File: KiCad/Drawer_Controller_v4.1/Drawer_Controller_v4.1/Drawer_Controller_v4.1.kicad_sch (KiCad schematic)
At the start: 21 parts, among them J1 Conn_02x05_Odd_Even, J2 Conn_02x03_Odd_Even, J3 Conn_02x04_Odd_Even, U1 PESD2CANFD24L-TR, X1 RJ45_45_degree_angled, X2 Conn_01x02_2.5mm_JST_S02B-XAS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, X3 Conn_01x08_2.5mm_JST_S04B-XAS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, X4 Conn_02x03_3.0mm_Molex_Micro_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, X5 Conn_01x03_2.5mm_JST_S04B-XAS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, X6 Conn_01x04_2.5mm_JST_S04B-XAS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

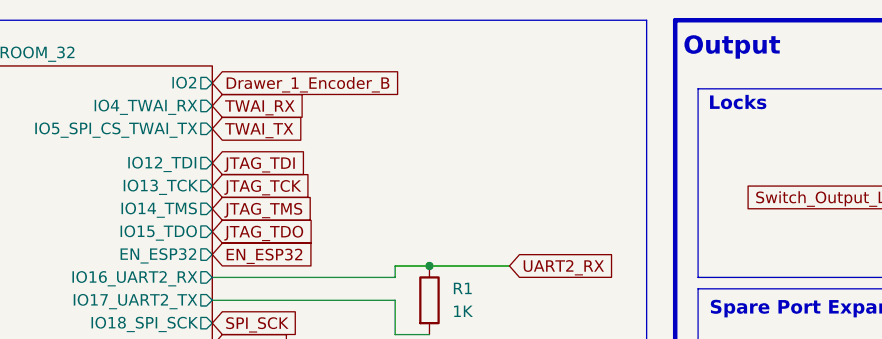
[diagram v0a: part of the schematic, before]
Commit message: fix: adds important hint about usage of IO2 for flashing the ESP32
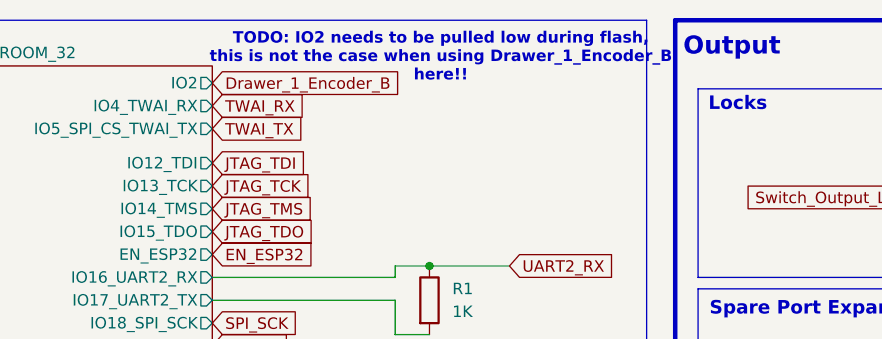
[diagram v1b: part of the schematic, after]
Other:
- note added: "TODO: IO2 needs to be pulled low during flash, this is not the case when using Drawer_1_Encoder_B here!!"
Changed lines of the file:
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@@
+		)
+	)
+	(text "TODO: IO2 needs to be pulled low during flash,\nthis is not the case when using Drawer_1_Encoder_B\nhere!!"
+		(exclude_from_sim no)
+		(at 219.71 18.796 0)
+		(effects
+			(font
+				(size 1.27 1.27)
+				(thickness 0.254)
+				(bold yes)
+				(color 255 0 0 1)
+			)
 		)
 	)

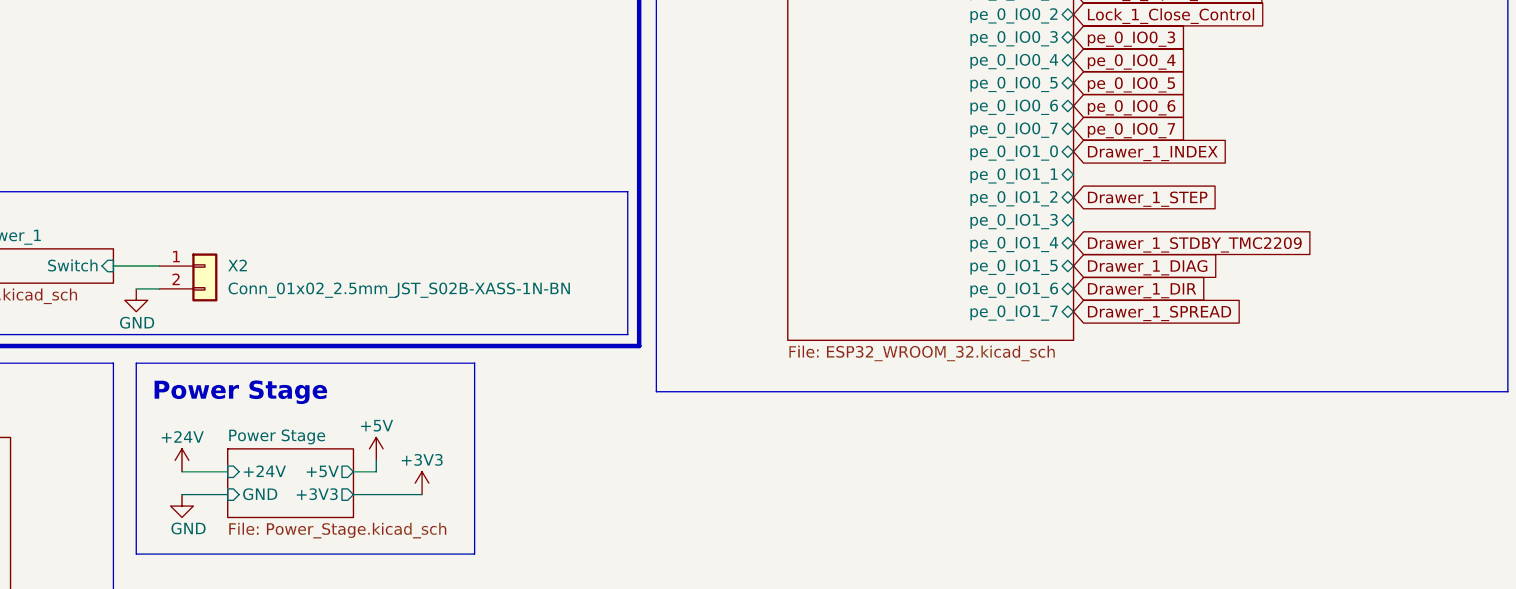
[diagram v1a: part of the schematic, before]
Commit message: fix: connects label `CAN_EN_High_Speed_Mode` and adds TODO for reverse polarity protection
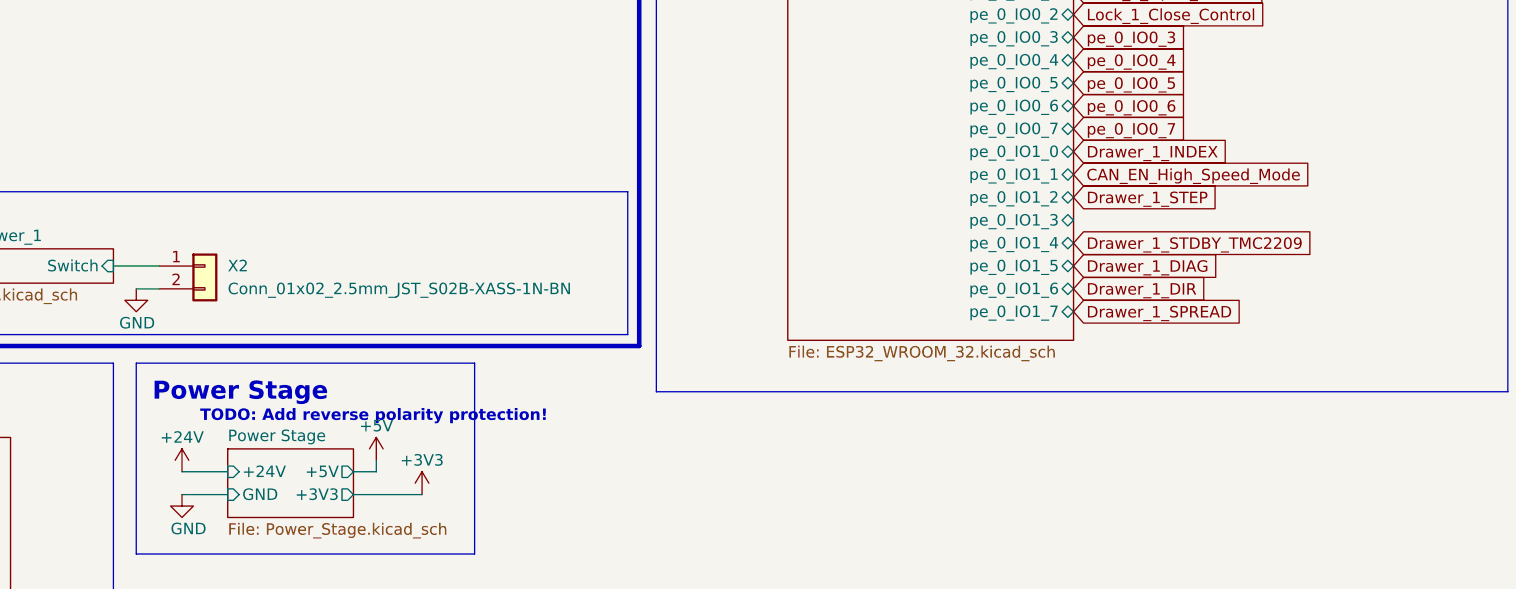
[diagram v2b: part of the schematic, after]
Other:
- note added: "TODO: Add reverse polarity protection!"
